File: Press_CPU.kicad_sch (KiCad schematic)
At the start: 104 parts

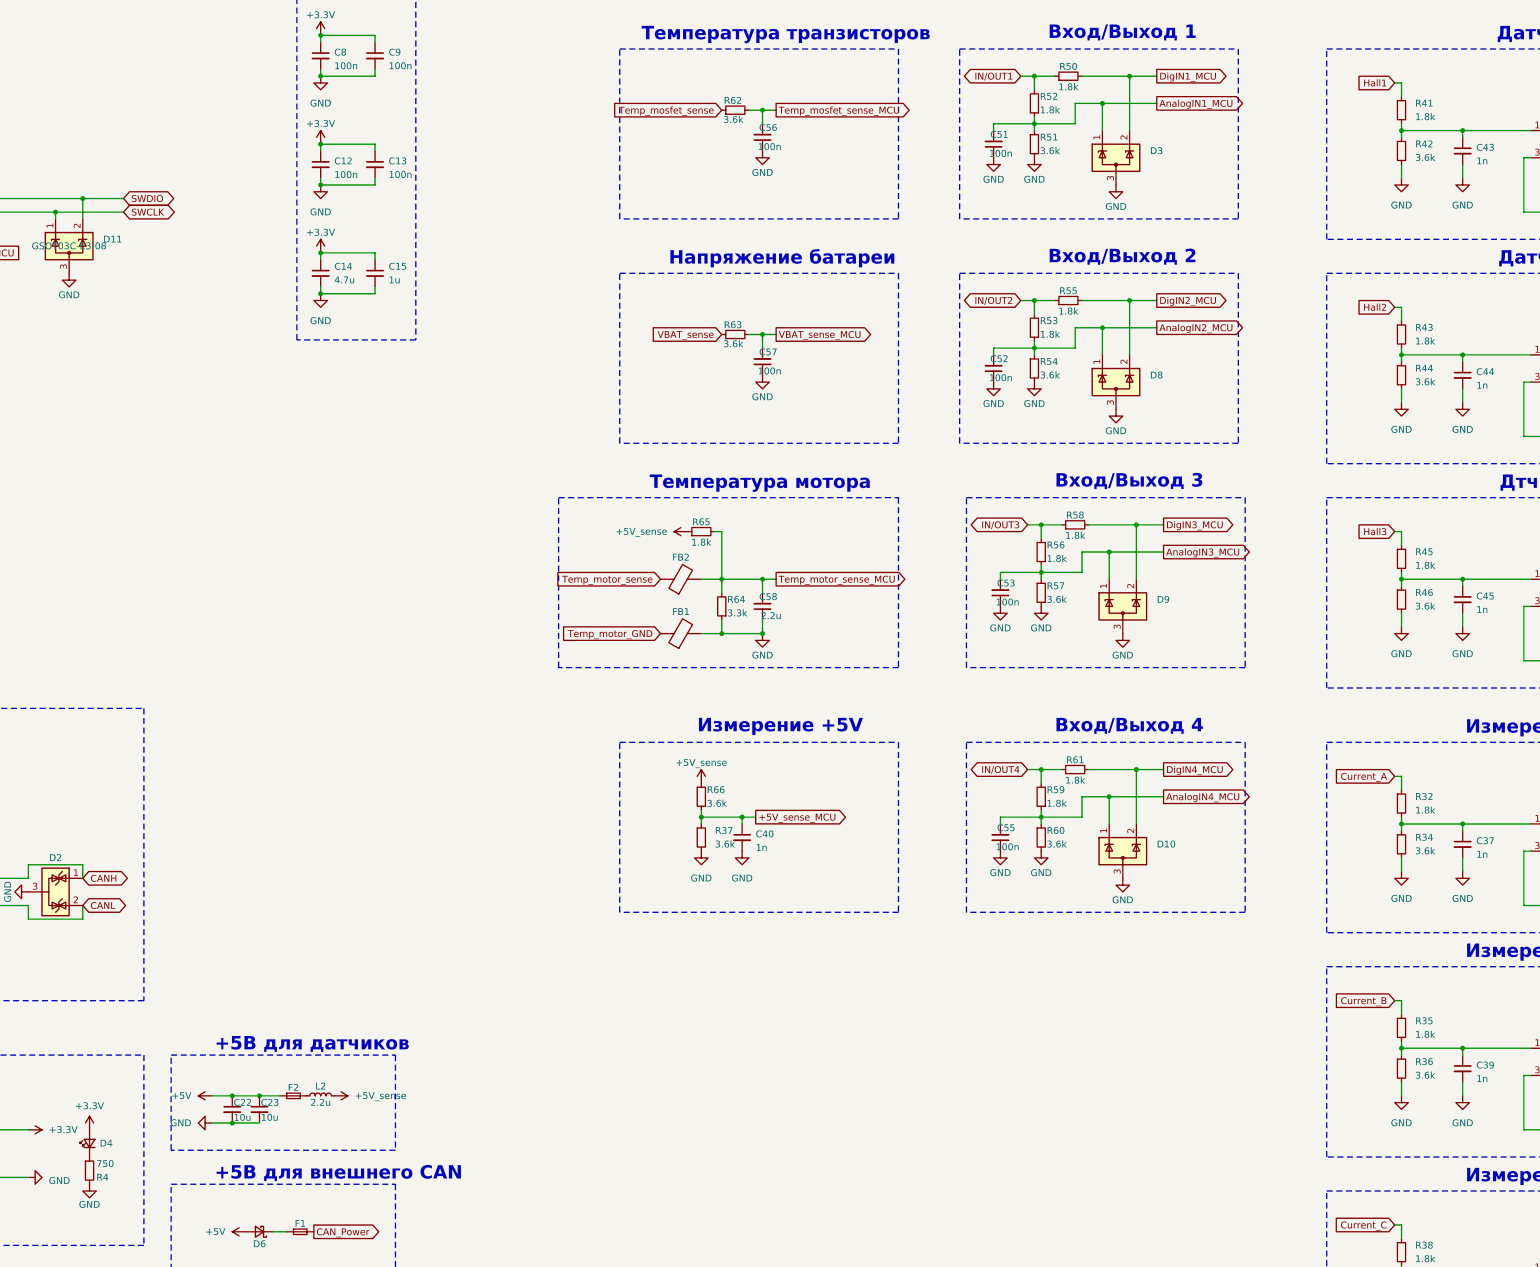
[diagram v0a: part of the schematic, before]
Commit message: VER1.0: отредактировал бом и обновил лист закупки
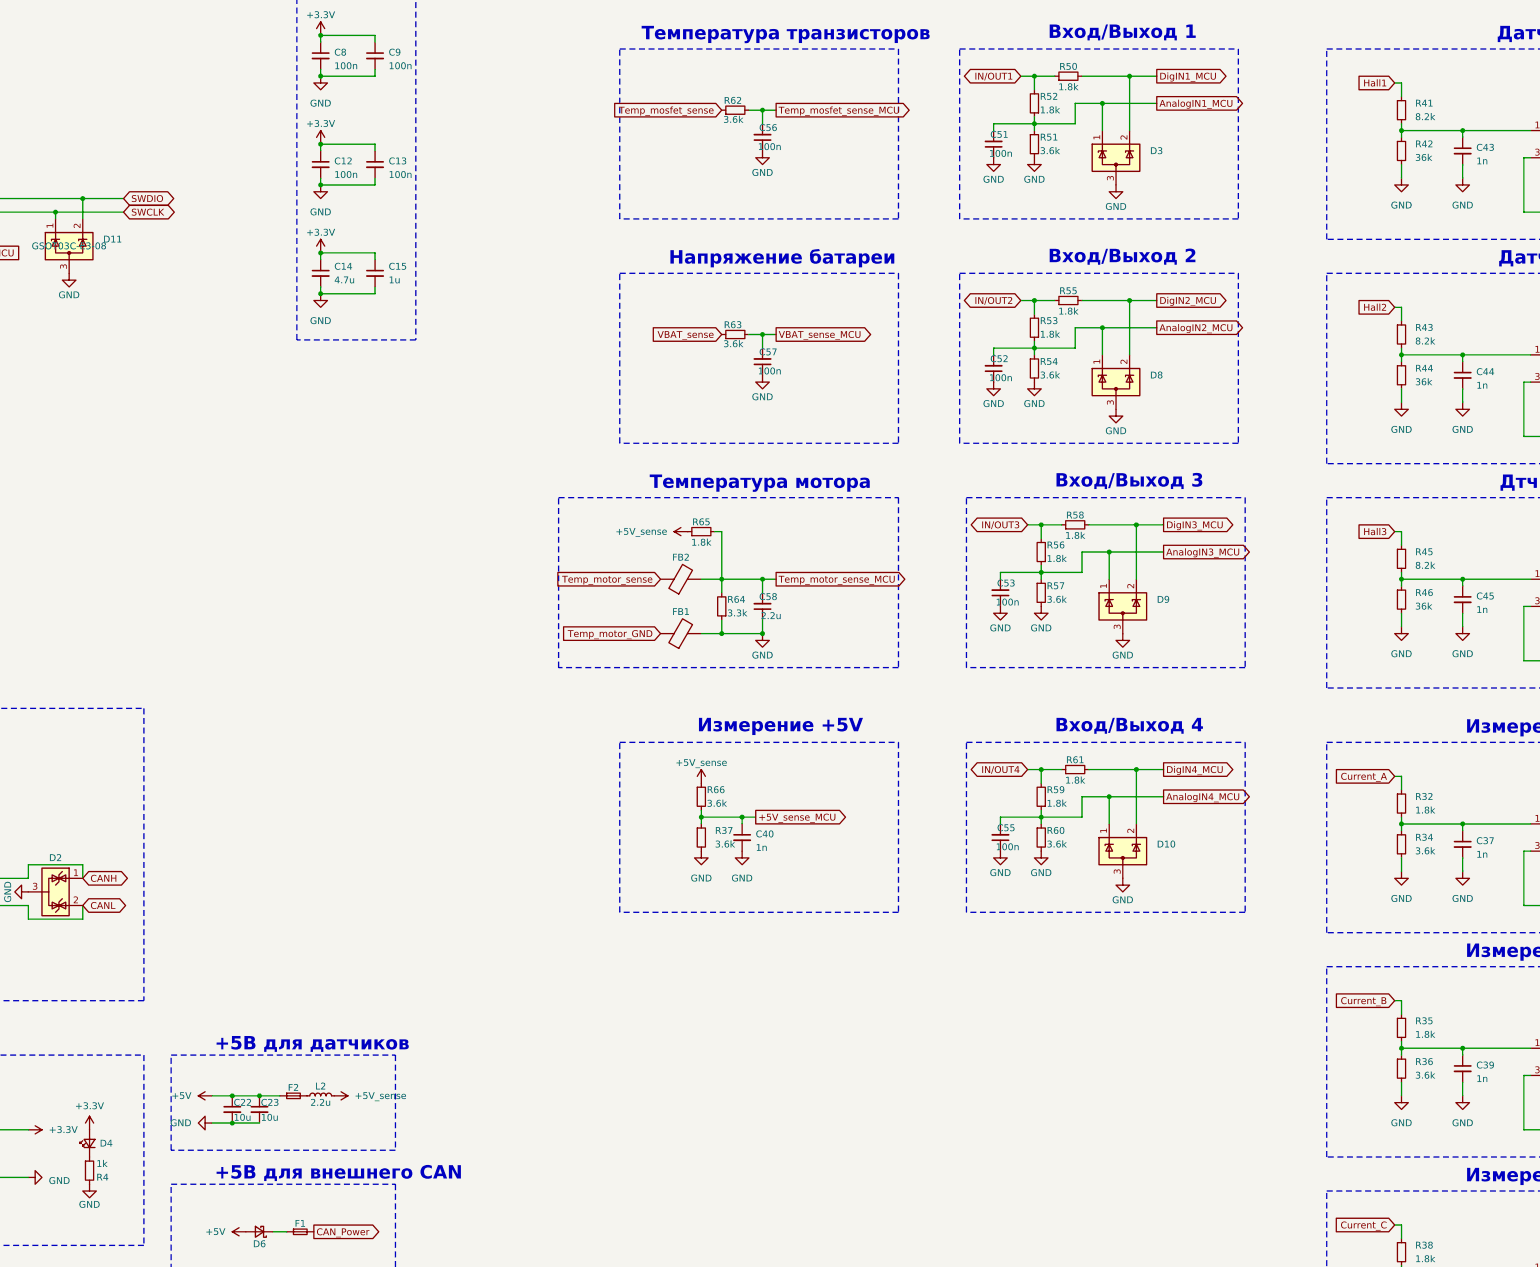
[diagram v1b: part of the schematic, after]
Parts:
- R4: value 750 -> 1k
- R41, R43, R45: value 1.8k -> 8.2k
- R42, R44, R46: value 3.6k -> 36k
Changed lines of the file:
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@@
 		(fields_autoplaced yes)
 		(property "Reference" "R45"
-			(at 506.73 212.09 0)
+			(at 506.73 212.0899 0)
 			(effects
 				(font
@@
 			)
 		)
-		(property "Value" "1.8k"
-			(at 506.73 214.63 0)
+		(property "Value" "8.2k"
+			(at 506.73 214.6299 0)
 			(effects
 				(font
@@
 		(fields_autoplaced yes)
 		(property "Reference" "R42"
-			(at 506.73 135.89 0)
+			(at 506.73 135.8899 0)
 			(effects
 				(font
@@
 			)
 		)
-		(property "Value" "3.6k"
-			(at 506.73 138.43 0)
+		(property "Value" "36k"
+			(at 506.73 138.4299 0)
 			(effects
 				(font
@@
 		(fields_autoplaced yes)
 		(property "Reference" "R41"
-			(at 506.73 128.27 0)
+			(at 506.73 128.2699 0)
 			(effects
 				(font
@@
 			)
 		)
-		(property "Value" "1.8k"
-			(at 506.73 130.81 0)
+		(property "Value" "8.2k"
+			(at 506.73 130.8099 0)
 			(effects
 				(font
@@
 		(fields_autoplaced yes)
 		(property "Reference" "R43"
-			(at 506.73 170.18 0)
+			(at 506.73 170.1799 0)
 			(effects
 				(font
@@
 			)
 		)
-		(property "Value" "1.8k"
-			(at 506.73 172.72 0)
+		(property "Value" "8.2k"
+			(at 506.73 172.7199 0)
 			(effects
 				(font
@@
 		(fields_autoplaced yes)
 		(property "Reference" "R44"
-			(at 506.73 177.8 0)
+			(at 506.73 177.7999 0)
 			(effects
 				(font
@@
 			)
 		)
-		(property "Value" "3.6k"
-			(at 506.73 180.34 0)
+		(property "Value" "36k"
+			(at 506.73 180.3399 0)
 			(effects
 				(font
@@
 		(fields_autoplaced yes)
 		(property "Reference" "R46"
-			(at 506.73 219.71 0)
+			(at 506.73 219.7099 0)
 			(effects
 				(font
@@
 			)
 		)
-		(property "Value" "3.6k"
-			(at 506.73 222.25 0)
+		(property "Value" "36k"
+			(at 506.73 222.2499 0)
 			(effects
 				(font
@@
 			)
 		)
-		(property "Value" "750"
+		(property "Value" "1k"
 			(at 260.35 326.39 0)
 			(effects
